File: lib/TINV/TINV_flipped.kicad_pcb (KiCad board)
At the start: 2 copper layers, 4 parts

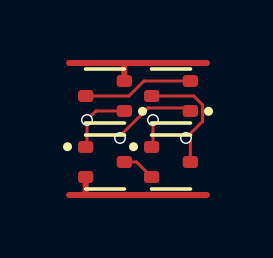
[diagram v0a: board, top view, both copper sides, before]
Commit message: All cells now use 1mm*4mm grid rather than 1.1mm*4.4mm
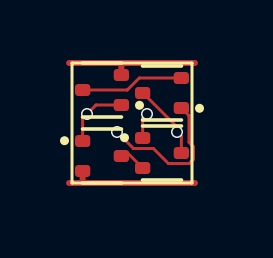
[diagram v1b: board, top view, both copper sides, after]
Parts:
- moved P2 0.42 mm to (3.00, 3.00)
- moved N2 0.32 mm to (3.00, 1.00)
- moved N1 0.22 mm to (1.00, 0.90)
- moved P1 0.22 mm to (1.00, 3.10)
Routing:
- net EN: track 2.84 -> 4.92 mm
- net Y: track 4.01 -> 2.54 mm
- net GND: track 5.22 -> 4.62 mm
- net VDD: track 5.20 -> 4.62 mm
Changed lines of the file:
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@@
 	(footprint "Package_TO_SOT_SMD:SOT-523"
 		(layer "F.Cu")
-		(at 3.3 1.1 180)
+		(at 3 1 180)
 		(descr "SOT523, https://www.diodes.com/assets/Package-Files/SOT523.pdf")
 		(tags "SOT-523")
@@
 	(footprint "Package_TO_SOT_SMD:SOT-523"
 		(layer "F.Cu")
-		(at 3.3 3.3)
+		(at 3 3)
 		(descr "SOT523, https://www.diodes.com/assets/Package-Files/SOT523.pdf")
 		(tags "SOT-523")
@@
 	(footprint "Package_TO_SOT_SMD:SOT-523"
 		(layer "F.Cu")
-		(at 1.1 1.1 180)
+		(at 1 0.9 180)
 		(descr "SOT523, https://www.diodes.com/assets/Package-Files/SOT523.pdf")
 		(tags "SOT-523")
@@
 	(footprint "Package_TO_SOT_SMD:SOT-523"
 		(layer "F.Cu")
-		(at 1.1 3.3)
+		(at 1 3.1)
 		(descr "SOT523, https://www.diodes.com/assets/Package-Files/SOT523.pdf")
 		(tags "SOT-523")
@@
 		)
 	)
-	(segment
-		(start 4.351 1.393262)
-		(end 4.351 1.949)
+	(gr_rect
+		(start 0 0)
+		(end 4 4)
+		(stroke
+			(width 0.1)
+			(type default)
+		)
+		(fill no)
+		(layer "F.SilkS")
+	)
+	(segment
+		(start 3.645 3)
+		(end 3.645 2.445)
 		(width 0.1)
 		(layer "F.Cu")
@@
 	)
 	(segment
-		(start 3.945 2.645)
-		(end 3.8 2.5)
+		(start 3.645 2.445)
+		(end 3.5 2.3)
 		(width 0.1)
 		(layer "F.Cu")
@@
 	)
 	(segment
-		(start 3.945 3.3)
-		(end 3.945 2.645)
+		(start 3.5 2.3)
+		(end 3.5 2.1329)
 		(width 0.1)
 		(layer "F.Cu")
@@
 	)
 	(segment
-		(start 4.057738 1.1)
-		(end 4.351 1.393262)
+		(start 2.3671 1)
+		(end 2.355 1)
 		(width 0.1)
 		(layer "F.Cu")
@@
 	)
 	(segment
-		(start 4.351 1.949)
-		(end 3.8 2.5)
+		(start 3.5 2.1329)
+		(end 2.3671 1)
 		(width 0.1)
 		(layer "F.Cu")
 		(net 1)
 	)
-	(segment
-		(start 2.655 1.1)
-		(end 4.057738 1.1)
-		(width 0.1)
-		(layer "F.Cu")
-		(net 1)
-	)
 	(via
-		(at 3.8 2.5)
+		(at 3.5 2.3)
 		(size 0.4)
 		(drill 0.3)
@@
 	)
 	(segment
-		(start 1.745 0.045)
-		(end 1.7 0)
+		(start 1.645 0.045)
+		(end 1.6 0)
 		(width 0.2)
 		(layer "F.Cu")
@@
 	)
 	(segment
-		(start 1.7 0)
-		(end 1.75 0)
+		(start 1.645 0.4)
+		(end 1.645 0.045)
 		(width 0.2)
 		(layer "F.Cu")
@@
 	(segment
 		(start -0.1 0)
-		(end 1.7 0)
+		(end 1.6 0)
 		(width 0.2)
 		(layer "F.Cu")
@@
 	)
 	(segment
-		(start 1.745 0.6)
-		(end 1.745 0.045)
+		(start 1.6 0)
+		(end 4.1 0)
 		(width 0.2)
 		(layer "F.Cu")
@@
 	)
 	(segment
-		(start 1.75 0)
-		(end 4.5 0)
-		(width 0.2)
-		(layer "F.Cu")
-		(net 2)
-	)
-	(segment
-		(start 0.5 1.9)
-		(end 0.5 2.755)
+		(start 0.355 1.845)
+		(end 0.5 1.7)
 		(width 0.1)
 		(layer "F.Cu")
@@
 	)
 	(segment
-		(start 0.8 1.6)
-		(end 0.5 1.9)
+		(start 0.355 2.5)
+		(end 0.355 1.845)
 		(width 0.1)
 		(layer "F.Cu")
@@
 	)
 	(segment
-		(start 0.5 2.755)
-		(end 0.455 2.8)
+		(start 1.645 1.4)
+		(end 0.8 1.4)
 		(width 0.1)
 		(layer "F.Cu")
@@
 	)
 	(segment
-		(start 1.745 1.6)
-		(end 0.8 1.6)
+		(start 0.8 1.4)
+		(end 0.5 1.7)
 		(width 0.1)
 		(layer "F.Cu")
@@
 	)
 	(via
-		(at 0.5 1.9)
+		(at 0.5 1.7)
 		(size 0.4)
 		(drill 0.3)
@@
 	)
 	(segment
-		(start 2.65 4.4)
-		(end 4.5 4.4)
+		(start 0.355 3.945)
+		(end 0.3 4)
 		(width 0.2)
 		(layer "F.Cu")
@@
 	)
 	(segment
-		(start 0.455 4.395)
-		(end 0.46 4.4)
+		(start 0.3 4)
+		(end 4.1 4)
 		(width 0.2)
 		(layer "F.Cu")
@@
 	)
 	(segment
-		(start 0.46 4.4)
-		(end 2.65 4.4)
+		(start 0.355 3.6)
+		(end 0.355 3.945)
 		(width 0.2)
 		(layer "F.Cu")
@@
 	)
 	(segment
-		(start 0.455 3.8)
-		(end 0.455 4.395)
+		(start -0.1 4)
+		(end 0.3 4)
 		(width 0.2)
 		(layer "F.Cu")
@@
 	)
 	(segment
-		(start -0.1 4.4)
-		(end 0.46 4.4)
-		(width 0.2)
-		(layer "F.Cu")
-		(net 4)
-	)
-	(segment
-		(start 2.4 0.6)
-		(end 1.9 1.1)
+		(start 0.355 0.9)
+		(end 1.842262 0.9)
 		(width 0.1)
 		(layer "F.Cu")
@@
 	)
 	(segment
-		(start 3.945 0.6)
-		(end 2.4 0.6)
+		(start 2.242262 0.5)
+		(end 3.645 0.5)
 		(width 0.1)
 		(layer "F.Cu")
@@
 	)
 	(segment
-		(start 1.9 1.1)
-		(end 0.455 1.1)
+		(start 1.842262 0.9)
+		(end 2.242262 0.5)
 		(width 0.1)
 		(layer "F.Cu")
@@
 	)
 	(segment
-		(start 3.844 1.499)
-		(end 3.945 1.6)
+		(start 3.2141 3.351)
+		(end 3.906738 3.351)
 		(width 0.1)
 		(layer "F.Cu")
@@
 	)
 	(segment
-		(start 2.5339 1.499)
-		(end 3.844 1.499)
+		(start 3.9 2.642262)
+		(end 3.9 1.755)
 		(width 0.1)
 		(layer "F.Cu")
@@
 	)
 	(segment
-		(start 1.6 2.4329)
-		(end 2.5339 1.499)
+		(start 2.051 2.851)
+		(end 2.7141 2.851)
 		(width 0.1)
 		(layer "F.Cu")
@@
 	)
 	(segment
-		(start 1.6 2.5)
-		(end 1.6 2.4329)
+		(start 3.906738 3.351)
+		(end 4.051 3.206738)
 		(width 0.1)
 		(layer "F.Cu")
 		(net 6)
 	)
+	(segment
+		(start 3.9 1.755)
+		(end 3.645 1.5)
+		(width 0.1)
+		(layer "F.Cu")
+		(net 6)
+	)
+	(segment
+		(start 4.051 3.206738)
+		(end 4.051 2.793262)
+		(width 0.1)
+		(layer "F.Cu")
+		(net 6)
+	)
+	(segment
+		(start 2.7141 2.851)
+		(end 3.2141 3.351)
+		(width 0.1)
+		(layer "F.Cu")
+		(net 6)
+	)
+	(segment
+		(start 1.5 2.3)
+		(end 2.051 2.851)
+		(width 0.1)
+		(layer "F.Cu")
+		(net 6)
+	)
+	(segment
+		(start 4.051 2.793262)
+		(end 3.9 2.642262)
+		(width 0.1)
+		(layer "F.Cu")
+		(net 6)
+	)
 	(via
-		(at 1.6 2.5)
+		(at 1.5 2.3)
 		(size 0.4)
 		(drill 0.3)
@@
 	)
 	(segment
-		(start 2.155 3.3)
-		(end 2.655 3.8)
+		(start 1.855 3)
+		(end 2.355 3.5)
 		(width 0.1)
 		(layer "F.Cu")
@@
 	)
 	(segment
-		(start 1.745 3.3)
-		(end 2.155 3.3)
+		(start 1.645 3)
+		(end 1.855 3)
 		(width 0.1)
 		(layer "F.Cu")
@@
 	)
 	(segment
-		(start 2.7 1.9)
-		(end 2.7 2.755)
+		(start 2.355 2.5)
+		(end 2.355 1.845)
 		(width 0.1)
 		(layer "F.Cu")
@@
 	)
 	(segment
-		(start 2.7 2.755)
-		(end 2.655 2.8)
+		(start 2.355 1.845)
+		(end 2.5 1.7)
 		(width 0.1)
 		(layer "F.Cu")
@@
 	)
 	(via
-		(at 2.7 1.9)
+		(at 2.5 1.7)
 		(size 0.4)
 		(drill 0.3)

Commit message: Make the pads of my SOT523 footprint very slightly smaller, which is enough to route all the cells and leave the mosfets exactly on the grid
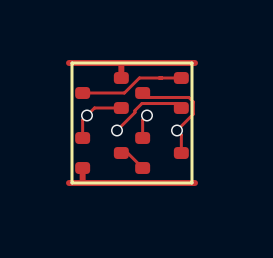
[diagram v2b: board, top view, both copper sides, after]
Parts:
- N1, N2, P1, P2: footprint Package_TO_SOT_SMD:SOT-523 -> RV523:SOT523
- moved P1 0.10 mm to (1.00, 3.00)
- moved N1 0.10 mm to (1.00, 1.00)
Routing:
- net EN: track 4.92 -> 2.62 mm
- net Y: track 2.54 -> 3.91 mm

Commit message: Propagate MOSFET values to the cells' PCBs
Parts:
- N1, N2: value (none) -> NMOS
- P1, P2: value (none) -> PMOS
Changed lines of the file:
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@@
 			)
 		)
-		(property "Value" ""
+		(property "Value" "NMOS"
 			(at 0 0 180)
 			(layer "F.Fab")
@@
 			)
 		)
-		(property "Value" ""
+		(property "Value" "PMOS"
 			(at 0 0 0)
 			(layer "F.Fab")
@@
 			)
 		)
-		(property "Value" ""
+		(property "Value" "NMOS"
 			(at 0 0 180)
 			(layer "F.Fab")
@@
 			)
 		)
-		(property "Value" ""
+		(property "Value" "PMOS"
 			(at 0 0 0)
 			(layer "F.Fab")
